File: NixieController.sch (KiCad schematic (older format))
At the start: 3 parts, among them J1 Jack-DC, J2 Conn_01x02_Male, J3 Conn_01x02_Male

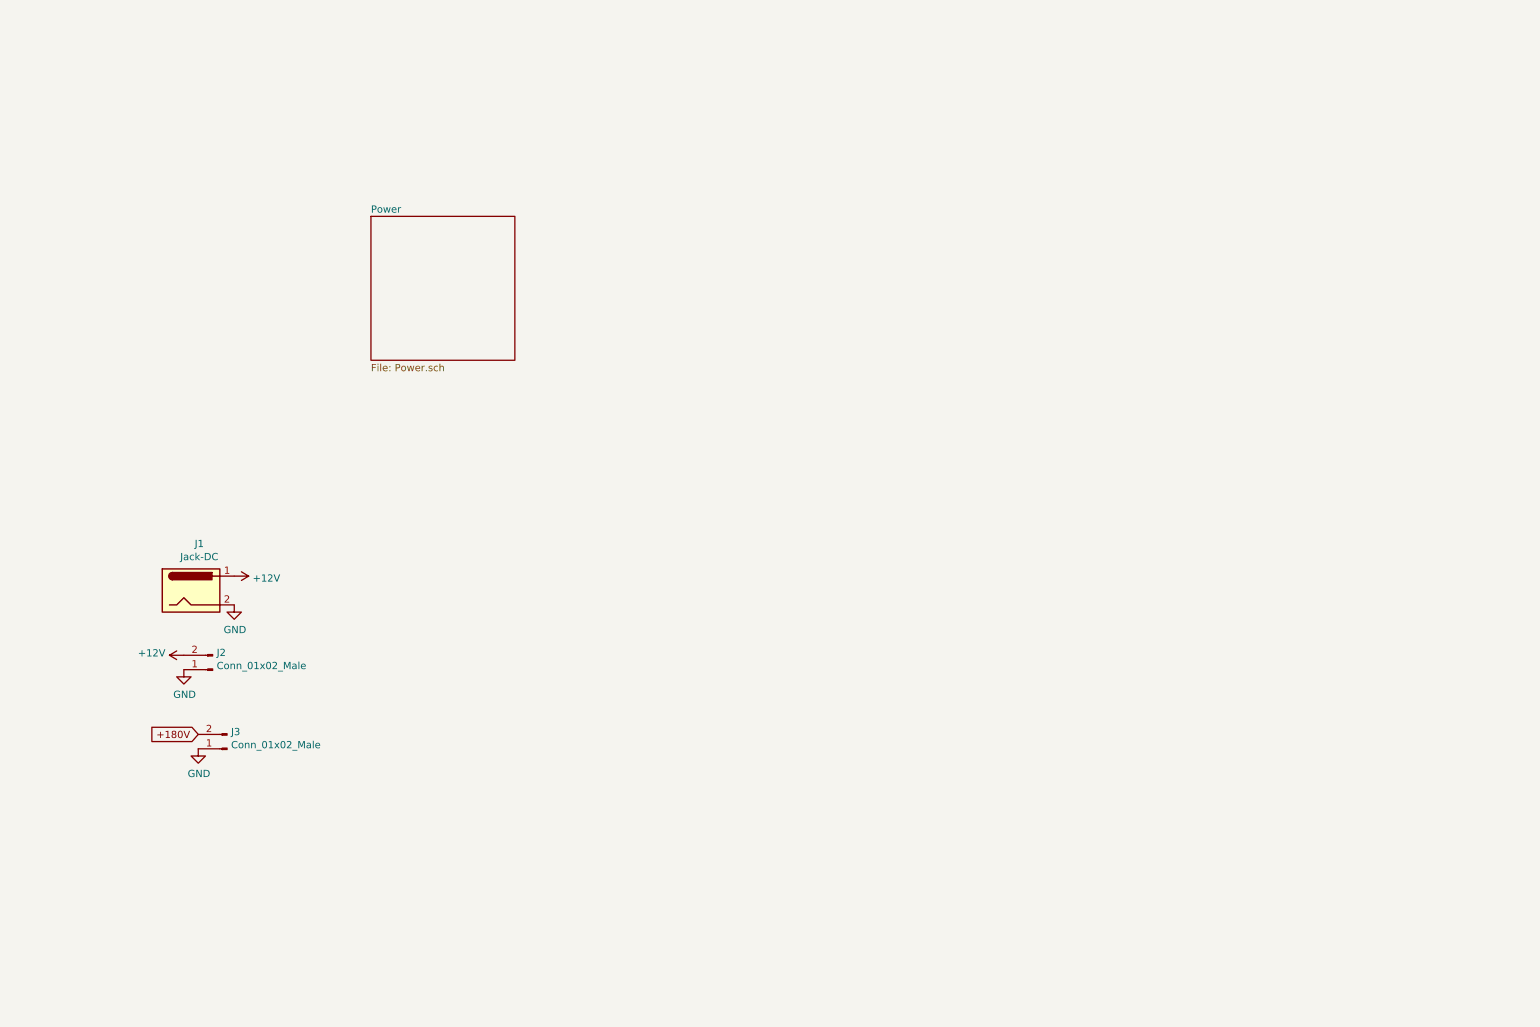
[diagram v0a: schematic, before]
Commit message: Completed entire board (not tested yet)
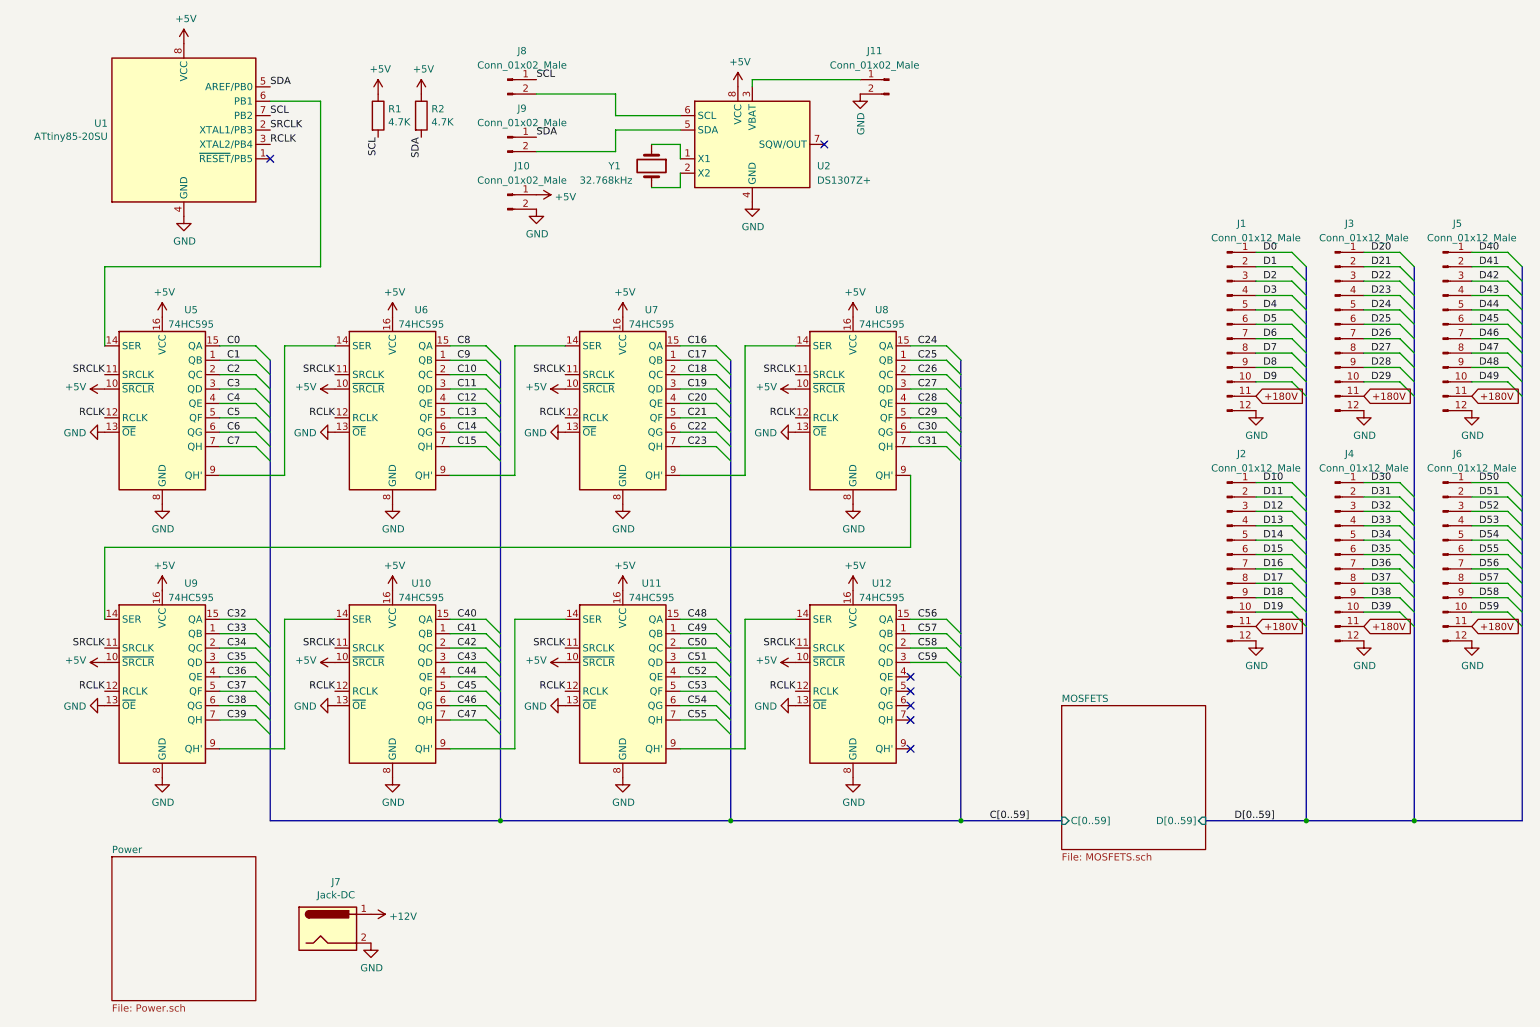
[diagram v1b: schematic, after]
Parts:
- removed J2, J3: Conn_01x02_Male, Connector_PinHeader_2.54mm:PinHeader_1x02_P2.54mm_Vertical, symbol Connector:Conn_01x02_Male
- added J1, J2, J3, J4, J5, J6: Conn_01x12_Male, Connector_PinHeader_2.54mm:PinHeader_1x12_P2.54mm_Vertical, symbol Connector:Conn_01x12_Male
- added J10, J11, J8, J9: Conn_01x02_Male, Connector_PinHeader_2.54mm:PinHeader_1x02_P2.54mm_Vertical, symbol Connector:Conn_01x02_Male
- added R1, R2: 4.7K, Resistor_SMD:R_0805_2012Metric, symbol Device:R
- added U1: ATtiny85-20SU, Package_SO:SOIC-8_5.275x5.275mm_P1.27mm, symbol MCU_Microchip_ATtiny:ATtiny85-20SU
- added U10, U11, U12, U5, U6, U7, U8, U9: 74HC595, Package_SO:SOIC-16_3.9x9.9mm_P1.27mm, symbol 74xx:74HC595
- added U2: DS1307Z+, Package_SO:SOIC-8_3.9x4.9mm_P1.27mm, symbol Timer_RTC:DS1307Z+
- added Y1: 32.768kHz, Crystal:Crystal_SMD_3215-2Pin_3.2x1.5mm, symbol Device:Crystal
- renumbered J1 to J7
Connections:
- net +180V: now also J1.11 (Pin_11), J2.11 (Pin_11), J3.11 (Pin_11), J4.11 (Pin_11), J5.11 (Pin_11), J6.11 (Pin_11)
- net GND: now also J1.12 (Pin_12), J10.2 (Pin_2), J11.2 (Pin_2), J2.12 (Pin_12), J3.12 (Pin_12), J4.12 (Pin_12), J5.12 (Pin_12), J6.12 (Pin_12), U1.4 (GND), U10.13 (~OE), U10.8 (GND), U11.13 (~OE), U11.8 (GND), U12.13 (~OE), U12.8 (GND), U2.4 (GND), U5.13 (~OE), U5.8 (GND), U6.13 (~OE), U6.8 (GND), U7.13 (~OE), U7.8 (GND), U8.13 (~OE), U8.8 (GND), U9.13 (~OE), U9.8 (GND)
- new net: U1.6 (PB1), U5.14 (SER)
- new net: U5.9 (QH'), U6.14 (SER)
- new net: U6.9 (QH'), U7.14 (SER)
- new net: U7.9 (QH'), U8.14 (SER)
- new net: U8.9 (QH'), U9.14 (SER)
- new net: U10.14 (SER), U9.9 (QH')
- new net: U10.9 (QH'), U11.14 (SER)
- new net: U11.9 (QH'), U12.14 (SER)
- new net: J8.2 (Pin_2), U2.6 (SCL)
- new net: J9.2 (Pin_2), U2.5 (SDA)
- new net: U2.1 (X1), Y1.1
- new net: U2.2 (X2), Y1.2
- new net: J11.1 (Pin_1), U2.3 (VBAT)
- new net +5V: J10.1 (Pin_1), R1.1, R2.1, U1.8 (VCC), U10.10 (~SRCLR), U10.16 (VCC), U11.10 (~SRCLR), U11.16 (VCC), U12.10 (~SRCLR), U12.16 (VCC), U2.8 (VCC), U5.10 (~SRCLR), U5.16 (VCC), U6.10 (~SRCLR), U6.16 (VCC), U7.10 (~SRCLR), U7.16 (VCC), U8.10 (~SRCLR), U8.16 (VCC), U9.10 (~SRCLR), U9.16 (VCC)
- new net C0: U5.15 (QA)
- new net C1: U5.1 (QB)
- new net C10: U6.2 (QC)
- new net C11: U6.3 (QD)
- new net C12: U6.4 (QE)
- new net C13: U6.5 (QF)
- new net C14: U6.6 (QG)
- new net C15: U6.7 (QH)
- new net C16: U7.15 (QA)
- new net C17: U7.1 (QB)
- new net C18: U7.2 (QC)
- new net C19: U7.3 (QD)
- new net C2: U5.2 (QC)
- new net C20: U7.4 (QE)
- new net C21: U7.5 (QF)
- new net C22: U7.6 (QG)
- new net C23: U7.7 (QH)
- new net C24: U8.15 (QA)
- new net C25: U8.1 (QB)
- new net C26: U8.2 (QC)
- new net C27: U8.3 (QD)
- new net C28: U8.4 (QE)
- new net C29: U8.5 (QF)
- new net C3: U5.3 (QD)
- new net C30: U8.6 (QG)
- new net C31: U8.7 (QH)
- new net C32: U9.15 (QA)
- new net C33: U9.1 (QB)
- new net C34: U9.2 (QC)
- new net C35: U9.3 (QD)
- new net C36: U9.4 (QE)
- new net C37: U9.5 (QF)
- new net C38: U9.6 (QG)
- new net C39: U9.7 (QH)
- new net C4: U5.4 (QE)
- new net C40: U10.15 (QA)
- new net C41: U10.1 (QB)
- new net C42: U10.2 (QC)
- new net C43: U10.3 (QD)
- new net C44: U10.4 (QE)
- new net C45: U10.5 (QF)
- new net C46: U10.6 (QG)
- new net C47: U10.7 (QH)
- new net C48: U11.15 (QA)
- new net C49: U11.1 (QB)
- new net C5: U5.5 (QF)
- new net C50: U11.2 (QC)
- new net C51: U11.3 (QD)
- new net C52: U11.4 (QE)
- new net C53: U11.5 (QF)
- new net C54: U11.6 (QG)
- new net C55: U11.7 (QH)
- new net C56: U12.15 (QA)
- new net C57: U12.1 (QB)
- new net C58: U12.2 (QC)
- new net C59: U12.3 (QD)
- new net C6: U5.6 (QG)
- new net C7: U5.7 (QH)
- new net C8: U6.15 (QA)
- new net C9: U6.1 (QB)
- new net D0: J1.1 (Pin_1)
- new net D1: J1.2 (Pin_2)
- new net D10: J2.1 (Pin_1)
- new net D11: J2.2 (Pin_2)
- new net D12: J2.3 (Pin_3)
- new net D13: J2.4 (Pin_4)
- new net D14: J2.5 (Pin_5)
- new net D15: J2.6 (Pin_6)
- new net D16: J2.7 (Pin_7)
- new net D17: J2.8 (Pin_8)
- new net D18: J2.9 (Pin_9)
- new net D19: J2.10 (Pin_10)
- new net D2: J1.3 (Pin_3)
- new net D20: J3.1 (Pin_1)
- new net D21: J3.2 (Pin_2)
- new net D22: J3.3 (Pin_3)
- new net D23: J3.4 (Pin_4)
- new net D24: J3.5 (Pin_5)
- new net D25: J3.6 (Pin_6)
- new net D26: J3.7 (Pin_7)
- new net D27: J3.8 (Pin_8)
- new net D28: J3.9 (Pin_9)
- new net D29: J3.10 (Pin_10)
- new net D3: J1.4 (Pin_4)
- new net D30: J4.1 (Pin_1)
- new net D31: J4.2 (Pin_2)
- new net D32: J4.3 (Pin_3)
- new net D33: J4.4 (Pin_4)
- new net D34: J4.5 (Pin_5)
- new net D35: J4.6 (Pin_6)
- new net D36: J4.7 (Pin_7)
- new net D37: J4.8 (Pin_8)
- new net D38: J4.9 (Pin_9)
- new net D39: J4.10 (Pin_10)
- new net D4: J1.5 (Pin_5)
- new net D40: J5.1 (Pin_1)
- new net D41: J5.2 (Pin_2)
- new net D42: J5.3 (Pin_3)
- new net D43: J5.4 (Pin_4)
- new net D44: J5.5 (Pin_5)
- new net D45: J5.6 (Pin_6)
- new net D46: J5.7 (Pin_7)
- new net D47: J5.8 (Pin_8)
- new net D48: J5.9 (Pin_9)
- new net D49: J5.10 (Pin_10)
- new net D5: J1.6 (Pin_6)
- new net D50: J6.1 (Pin_1)
- new net D51: J6.2 (Pin_2)
- new net D52: J6.3 (Pin_3)
- new net D53: J6.4 (Pin_4)
- new net D54: J6.5 (Pin_5)
- new net D55: J6.6 (Pin_6)
- new net D56: J6.7 (Pin_7)
- new net D57: J6.8 (Pin_8)
- new net D58: J6.9 (Pin_9)
- new net D59: J6.10 (Pin_10)
- new net D6: J1.7 (Pin_7)
- new net D7: J1.8 (Pin_8)
- new net D8: J1.9 (Pin_9)
- new net D9: J1.10 (Pin_10)
- new net RCLK: U1.3 (XTAL2/PB4), U10.12 (RCLK), U11.12 (RCLK), U12.12 (RCLK), U5.12 (RCLK), U6.12 (RCLK), U7.12 (RCLK), U8.12 (RCLK), U9.12 (RCLK)
- new net SCL: J8.1 (Pin_1), R1.2, U1.7 (PB2)
- new net SDA: J9.1 (Pin_1), R2.2, U1.5 (AREF/PB0)
- new net SRCLK: U1.2 (XTAL1/PB3), U10.11 (SRCLK), U11.11 (SRCLK), U12.11 (SRCLK), U5.11 (SRCLK), U6.11 (SRCLK), U7.11 (SRCLK), U8.11 (SRCLK), U9.11 (SRCLK)
- no-connect marks 0 -> 7
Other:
- moved on the sheet: J7

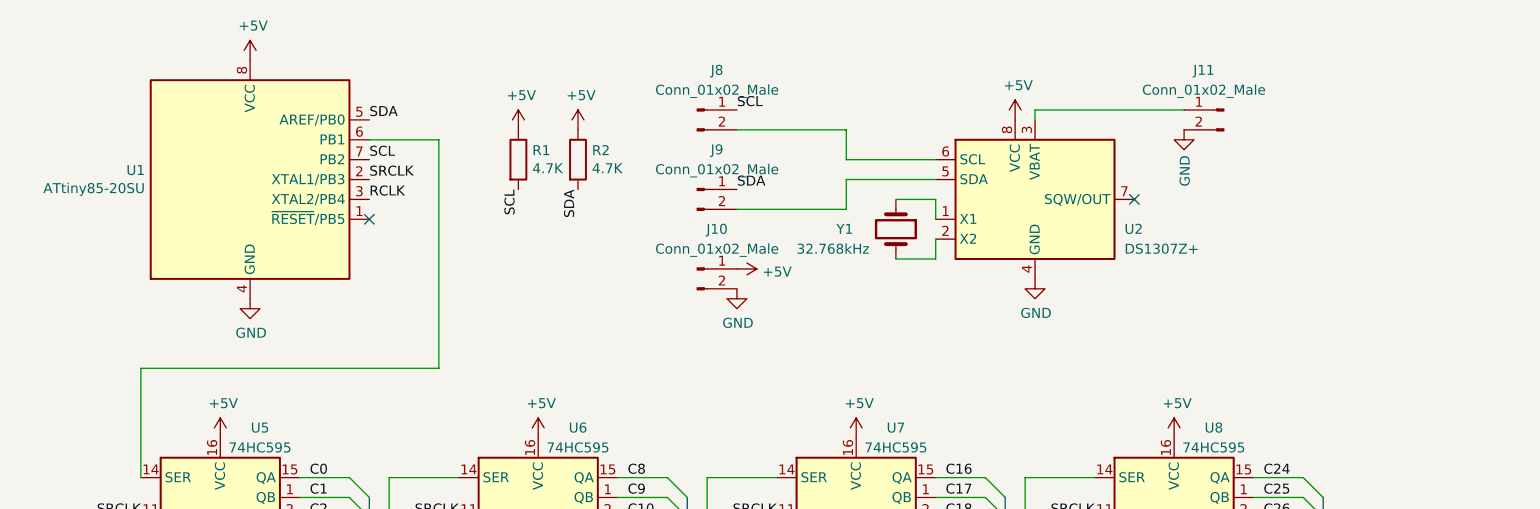
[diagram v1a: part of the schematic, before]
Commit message: Add ICSP for ucontroller, remove access to I2C
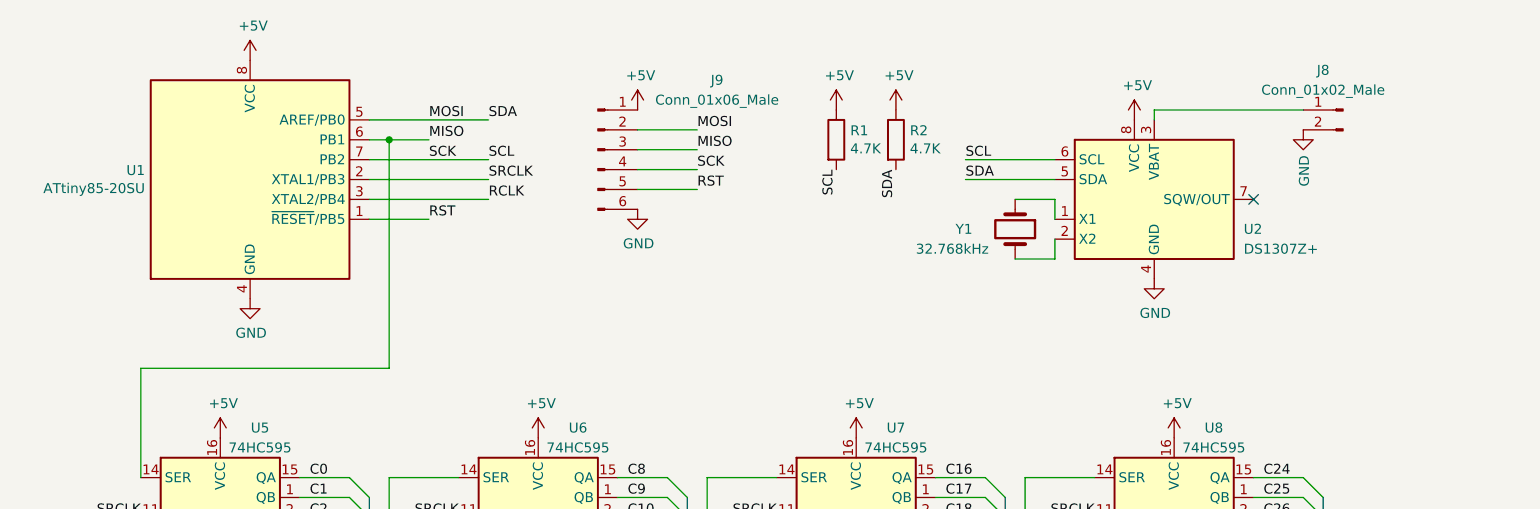
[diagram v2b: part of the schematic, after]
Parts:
- removed J10, J8, J9: Conn_01x02_Male, Connector_PinHeader_2.54mm:PinHeader_1x02_P2.54mm_Vertical, symbol Connector:Conn_01x02_Male
- added J9: Conn_01x06_Male, Connector_PinHeader_2.54mm:PinHeader_1x06_P2.54mm_Vertical, symbol Connector:Conn_01x06_Male
- renumbered J11 to J8
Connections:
- net SCL is gone; now on net SCK: R1.2, U1.7 (PB2)
- net SDA is gone; now on net MOSI: R2.2, U1.5 (AREF/PB0)
- net +5V: now also J9.1 (Pin_1)
- net GND: now also J9.6 (Pin_6)
- net RST: now reaches U1.1 (~RESET~/PB5)
- net RST: now also J9.5 (Pin_5)
- net MISO: now reaches U1.6 (PB1), U5.14 (SER)
- net MISO: now also J9.3 (Pin_3)
- net SCK: now reaches U2.6 (SCL)
- net SCK: now also J9.4 (Pin_4)
- net MOSI: now reaches U2.5 (SDA)
- net MOSI: now also J9.2 (Pin_2)
- no-connect marks 7 -> 6
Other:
- moved on the sheet: J8, R1, R2, U2, Y1
